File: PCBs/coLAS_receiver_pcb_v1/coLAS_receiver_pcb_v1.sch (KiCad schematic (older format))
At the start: 22 parts, among them J1 Conn_01x10_Female, J2 USB_B_Micro, U1 pic32mx274, U2 TSOP6238TT, U3 TSV914, U4 LM1117-3.3

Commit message: finished adding all foorprints, ready for routing
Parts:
- LS1: footprint (none) -> kicad_footprints:Multicomp_ultrasonic_transceiver
- U2: footprint (none) -> kicad_footprints:TSOP6238TT _IR_Receiver
- U3: footprint (none) -> Package_SO:SOIC-14_3.9x8.7mm_P1.27mm
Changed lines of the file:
@@
 F 0 "U3" H 2850 2117 50  0000 C CNN
 F 1 "TSV914" H 2850 2026 50  0000 C CNN
-F 2 "" H 2800 1850 50  0001 C CNN
+F 2 "Package_SO:SOIC-14_3.9x8.7mm_P1.27mm" H 2800 1850 50  0001 C CNN
 F 3 "www.st.com/resource/en/datasheet/tsv911.pdf" H 2900 1950 50  0001 C CNN
 	1    2850 1750
@@
 F 0 "U3" H 4400 2017 50  0000 C CNN
 F 1 "TSV914" H 4400 1926 50  0000 C CNN
-F 2 "" H 4350 1750 50  0001 C CNN
+F 2 "Package_SO:SOIC-14_3.9x8.7mm_P1.27mm" H 4350 1750 50  0001 C CNN
 F 3 "www.st.com/resource/en/datasheet/tsv911.pdf" H 4450 1850 50  0001 C CNN
 	2    4400 1650
@@
 F 0 "U3" H 6050 1917 50  0000 C CNN
 F 1 "TSV914" H 6050 1826 50  0000 C CNN
-F 2 "" H 6000 1650 50  0001 C CNN
+F 2 "Package_SO:SOIC-14_3.9x8.7mm_P1.27mm" H 6000 1650 50  0001 C CNN
 F 3 "www.st.com/resource/en/datasheet/tsv911.pdf" H 6100 1750 50  0001 C CNN
 	3    6050 1550
@@
 F 0 "LS1" H 2124 2246 50  0000 L CNN
 F 1 "Speaker_Ultrasound" H 2124 2155 50  0000 L CNN
-F 2 "" H 1915 2200 50  0001 C CNN
+F 2 "kicad_footprints:Multicomp_ultrasonic_transceiver" H 1915 2200 50  0001 C CNN
 F 3 "~" H 1915 2200 50  0001 C CNN
 	1    1950 2250
@@
 F 0 "U3" H 9058 1296 50  0000 L CNN
 F 1 "TSV914" H 9058 1205 50  0000 L CNN
-F 2 "" H 9050 1350 50  0001 C CNN
+F 2 "Package_SO:SOIC-14_3.9x8.7mm_P1.27mm" H 9050 1350 50  0001 C CNN
 F 3 "www.st.com/resource/en/datasheet/tsv911.pdf" H 9150 1450 50  0001 C CNN
 	5    9100 1250
@@
 F 0 "U3" H 7650 1083 50  0000 C CNN
 F 1 "TSV914" H 7650 1174 50  0000 C CNN
-F 2 "" H 7600 1550 50  0001 C CNN
+F 2 "Package_SO:SOIC-14_3.9x8.7mm_P1.27mm" H 7600 1550 50  0001 C CNN
 F 3 "www.st.com/resource/en/datasheet/tsv911.pdf" H 7700 1650 50  0001 C CNN
 	4    7650 1450
@@
 F 0 "U2" H 1888 3925 50  0000 C CNN
 F 1 "TSOP6238TT" H 1888 3834 50  0000 C CNN
-F 2 "" H 1850 3500 50  0001 C CNN
+F 2 "kicad_footprints:TSOP6238TT _IR_Receiver" H 1850 3500 50  0001 C CNN
 F 3 "" H 1850 3500 50  0001 C CNN
 	1    1850 3500

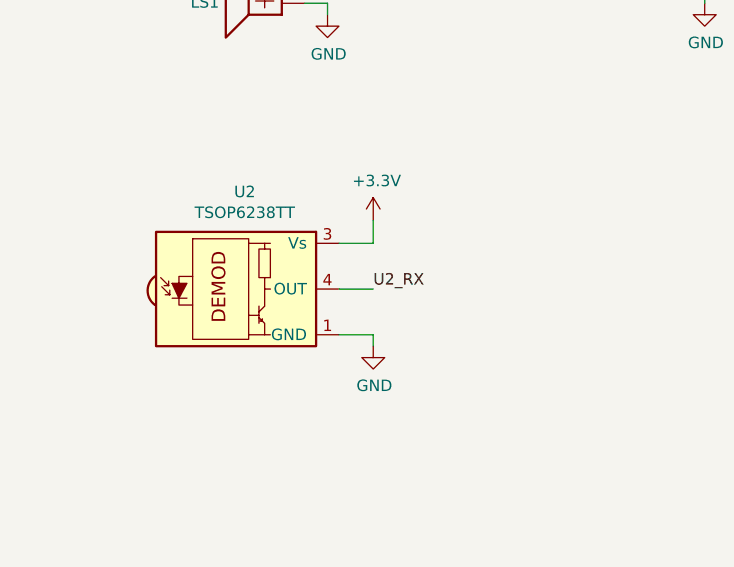
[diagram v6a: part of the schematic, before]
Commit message: changed ir receiver to through hole version
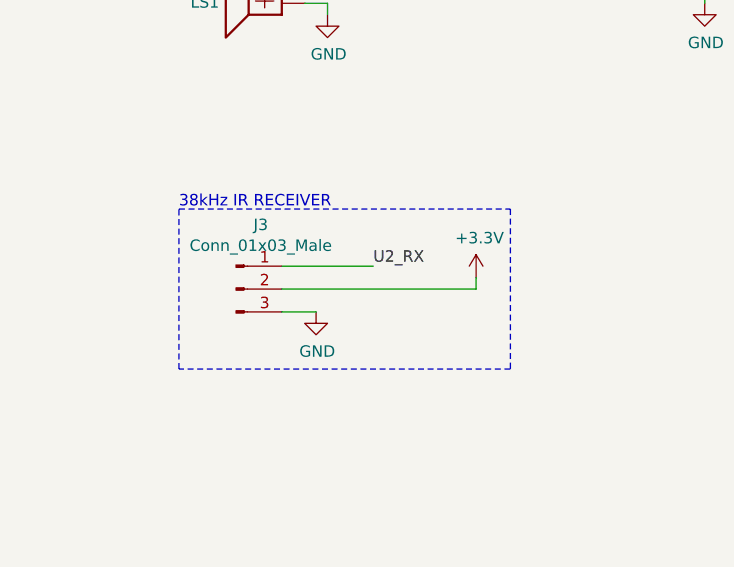
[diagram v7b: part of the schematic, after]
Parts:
- removed U2: TSOP6238TT, kicad_footprints:TSOP6238TT _IR_Receiver, symbol Kicad_symbols:TSOP6238TT
- added J3: Conn_01x03_Male, symbol Connector:Conn_01x03_Male
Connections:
- net +3V3: now also J3.2 (Pin_2)
- net GND: now also J3.3 (Pin_3)
- net U2_RX: now also J3.1 (Pin_1)
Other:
- note added: "38kHz IR RECEIVER\n"
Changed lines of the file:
@@
 	5050 4050 5200 4050
 $Comp
-L Kicad_symbols:TSOP6238TT U2
-U 1 1 5EA0D464
+L power:GND #PWR0118
+U 1 1 5EA12DBD
+P 2200 3600
+F 0 "#PWR0118" H 2200 3350 50  0001 C CNN
+F 1 "GND" H 2205 3427 50  0000 C CNN
+F 2 "" H 2200 3600 50  0001 C CNN
+F 3 "" H 2200 3600 50  0001 C CNN
+	1    2200 3600
+	1    0    0    -1
+$EndComp
+Text Label 2450 3400 0    50   ~ 0
+U2_RX
+$Comp
+L Connector:Conn_01x03_Male J3
+U 1 1 5ECE963B
 P 1850 3500
-F 0 "U2" H 1888 3925 50  0000 C CNN
-F 1 "TSOP6238TT" H 1888 3834 50  0000 C CNN
-F 2 "kicad_footprints:TSOP6238TT _IR_Receiver" H 1850 3500 50  0001 C CNN
-F 3 "" H 1850 3500 50  0001 C CNN
+F 0 "J3" H 1958 3781 50  0000 C CNN
+F 1 "Conn_01x03_Male" H 1958 3690 50  0000 C CNN
+F 2 "" H 1850 3500 50  0001 C CNN
+F 3 "~" H 1850 3500 50  0001 C CNN
 	1    1850 3500
 	1    0    0    -1
 $EndComp
+Wire Wire Line
+	2050 3400 2450 3400
+Wire Wire Line
+	2050 3600 2200 3600
+Wire Wire Line
+	2050 3500 2900 3500
+Wire Wire Line
+	2900 3500 2900 3450
 $Comp
 L power:+3.3V #PWR0117
-U 1 1 5EA1248E
-P 2450 3200
-F 0 "#PWR0117" H 2450 3050 50  0001 C CNN
-F 1 "+3.3V" H 2465 3373 50  0000 C CNN
-F 2 "" H 2450 3200 50  0001 C CNN
-F 3 "" H 2450 3200 50  0001 C CNN
-	1    2450 3200
+U 1 1 5ECF42D7
+P 2900 3450
+F 0 "#PWR0117" H 2900 3300 50  0001 C CNN
+F 1 "+3.3V" H 2915 3623 50  0000 C CNN
+F 2 "" H 2900 3450 50  0001 C CNN
+F 3 "" H 2900 3450 50  0001 C CNN
+	1    2900 3450
 	1    0    0    -1
 $EndComp
-$Comp
-L power:GND #PWR0118
-U 1 1 5EA12DBD
-P 2450 3750
-F 0 "#PWR0118" H 2450 3500 50  0001 C CNN
-F 1 "GND" H 2455 3577 50  0000 C CNN
-F 2 "" H 2450 3750 50  0001 C CNN
-F 3 "" H 2450 3750 50  0001 C CNN
-	1    2450 3750
-	1    0    0    -1
-$EndComp
-Wire Wire Line
-	2300 3300 2450 3300
-Wire Wire Line
-	2450 3300 2450 3200
-Wire Wire Line
-	2300 3700 2450 3700
-Wire Wire Line
-	2450 3700 2450 3750
-Text Label 2450 3500 0    50   ~ 0
-U2_RX
-Wire Wire Line
-	2300 3500 2450 3500
+Wire Notes Line
+	1600 3150 3050 3150
+Wire Notes Line
+	3050 3150 3050 3850
+Wire Notes Line
+	3050 3850 1600 3850
+Wire Notes Line
+	1600 3850 1600 3150
+Text Notes 1600 3150 0    50   ~ 0
+38kHz IR RECEIVER\n
 $EndSCHEMATC
